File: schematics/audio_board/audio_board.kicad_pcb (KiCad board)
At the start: 2 copper layers, 50 x 50 mm, 73 parts, among them J1 pyr ctrl, J2 mic, J3 power, J4 pyr ctrl, J6 pyr in, J7 audio ctrl, J8 speaker, Q1 bc847, Q2 bc847, Q3 dgm2305ux, Q7 dgm2305ux, U1 TPS613222ADBV, U2 MCP1802x-xx02xOT, U3 MCP1802x-xx02xOT, U4 TPS613222ADBV, U5 PAM8302AAD, U6 TLV9061xDBV, U7 TLV9061xDBV

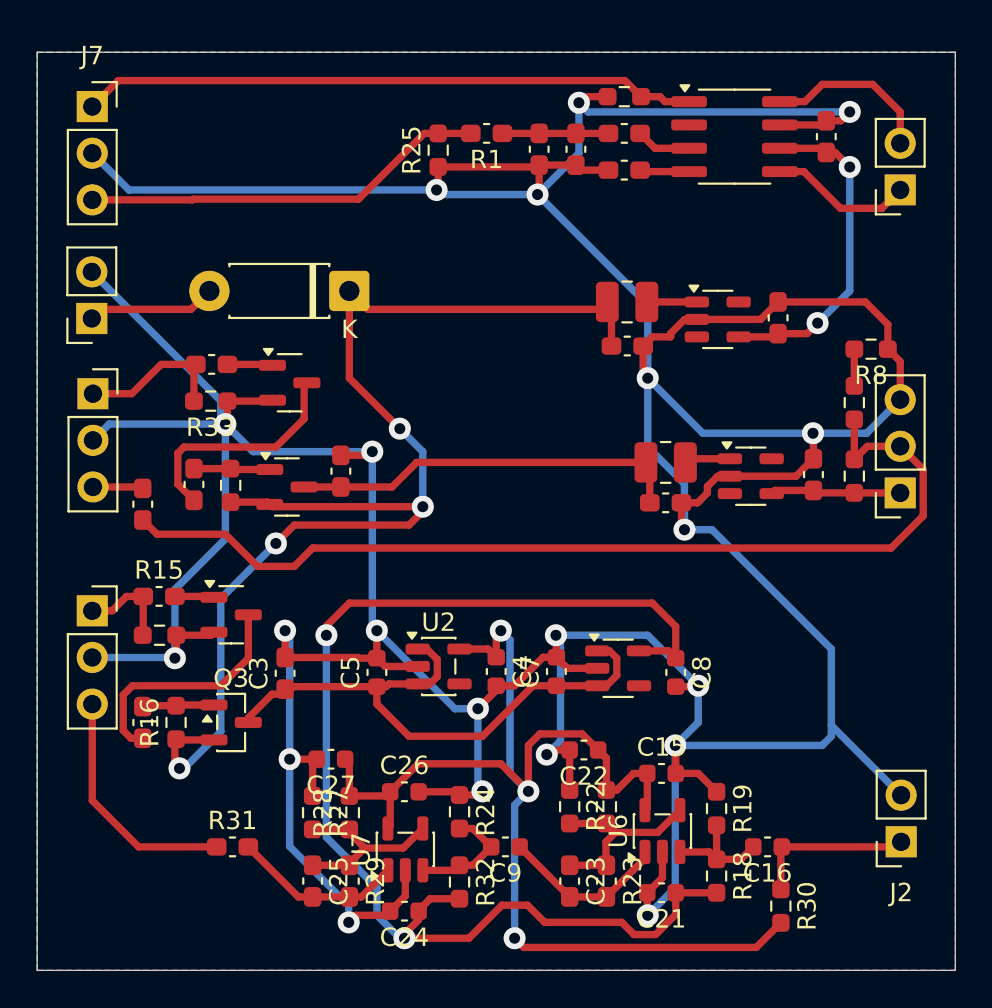
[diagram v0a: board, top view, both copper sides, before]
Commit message: Added ground via stitching. Generated new BOM.
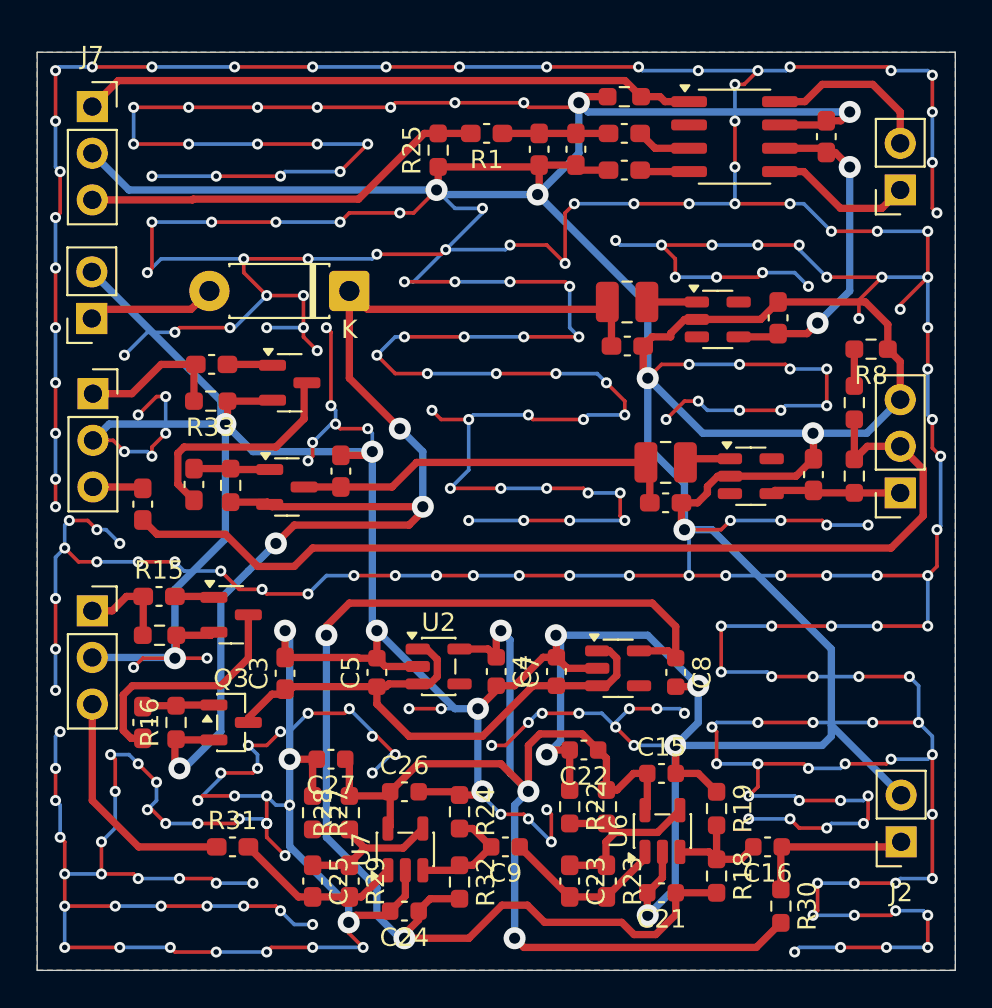
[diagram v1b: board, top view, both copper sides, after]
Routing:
- net GND: track 332.2 -> 1043.3 mm, vias 21 -> 299

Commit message: Correct package for audio amplifier. It is MSOP-8, not SOIC-8.
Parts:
- U5: footprint Package_SO:SOIC-8_3.9x4.9mm_P1.27mm -> Package_SO:MSOP-8_3x3mm_P0.65mm
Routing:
- net Net-(U5-IN-): track 2.70 -> 3.49 mm
- net Net-(J8-Pin_2): track 9.27 -> 10.0 mm
- net Net-(J8-Pin_1): track 7.79 -> 8.54 mm
- net /audio_en: track 33.6 -> 34.3 mm
